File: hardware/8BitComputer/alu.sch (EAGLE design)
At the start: 32 parts, among them IC1 SN74LS245NE4, IC2 SN74LS86AN, IC3 SN74LS283N, IC4 SN74LS86AN, IC8 SN74LS283N

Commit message: alu routed
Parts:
- added LED9: RED, leds:LED-3MM-NO_SILK
- added R9: 100 R, passives:RESISTOR0805-RES
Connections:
- removed net N$6: J5.5
- new net N$10: IC3.C4, R9.1
- new net N$11: LED9.A, R9.2
- net ALUOUT_OE: now also J5.3; no longer J5.2
- net AO_DIR: now also J5.2; no longer J5.3
- net AR2O_2: now also IC8.B3
- net AR2O_3: no longer IC8.B3
- net CARRY_ADD: now also IC3.C0, IC8.C4; no longer IC3.C4, IC8.C0
- net GND: now also J5.5, LED9.C
- net OP_SUBTRACT: now also IC8.C0; no longer IC8.C4
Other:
- note added: "C4 = carry out We subtract by using the 2's compliment, so we need to add one after we create the 1 compliement. X - Y = X + (~Y+1)"
- note removed: "C4 = carry In We subtract by using the 2's compliment, so we need to add one after we create the 1 compliement. X - Y = X + (~Y+1)"
- moved on the sheet: J2

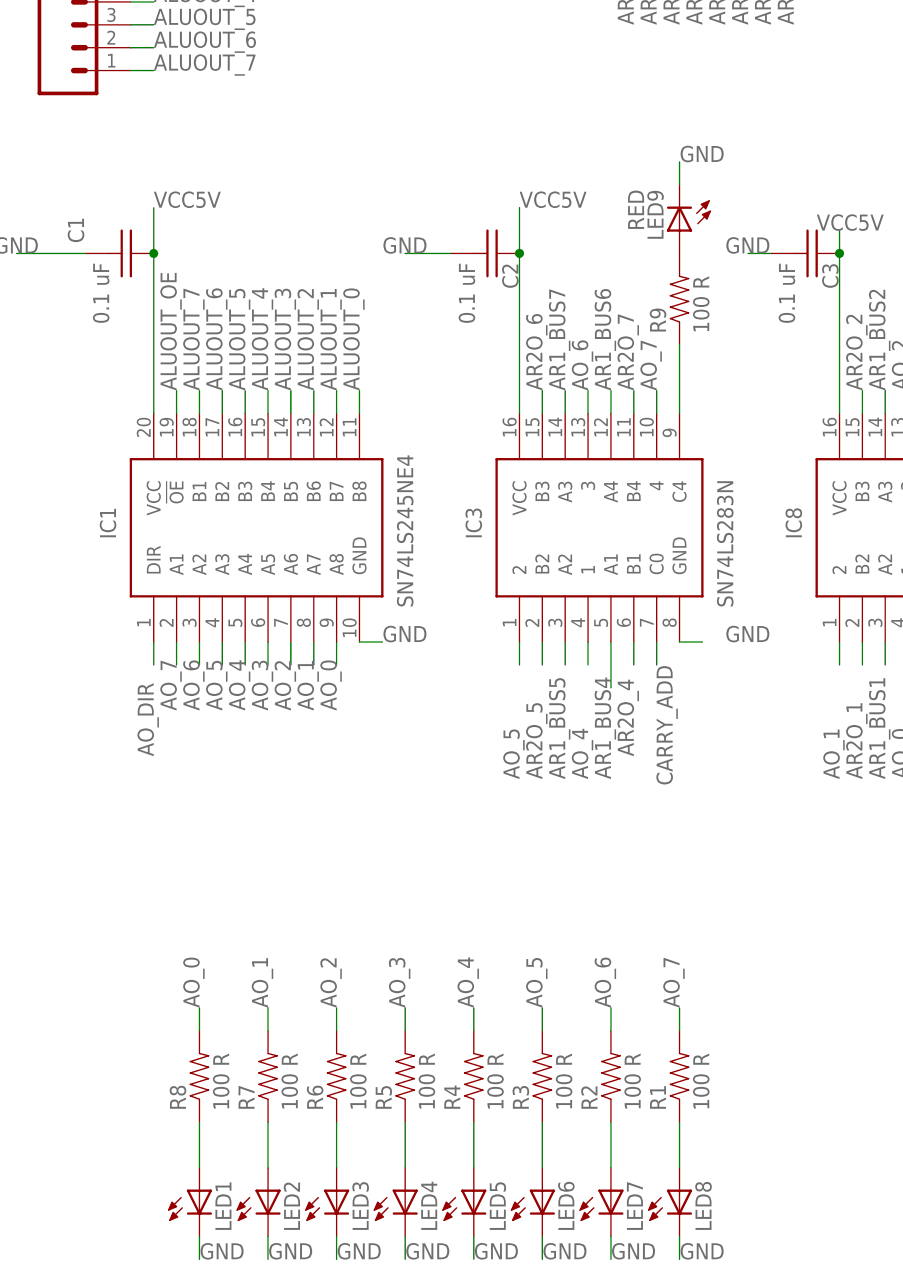
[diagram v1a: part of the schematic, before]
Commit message: adding static ram chip updated all other boards to remove led resistors that aren't needed
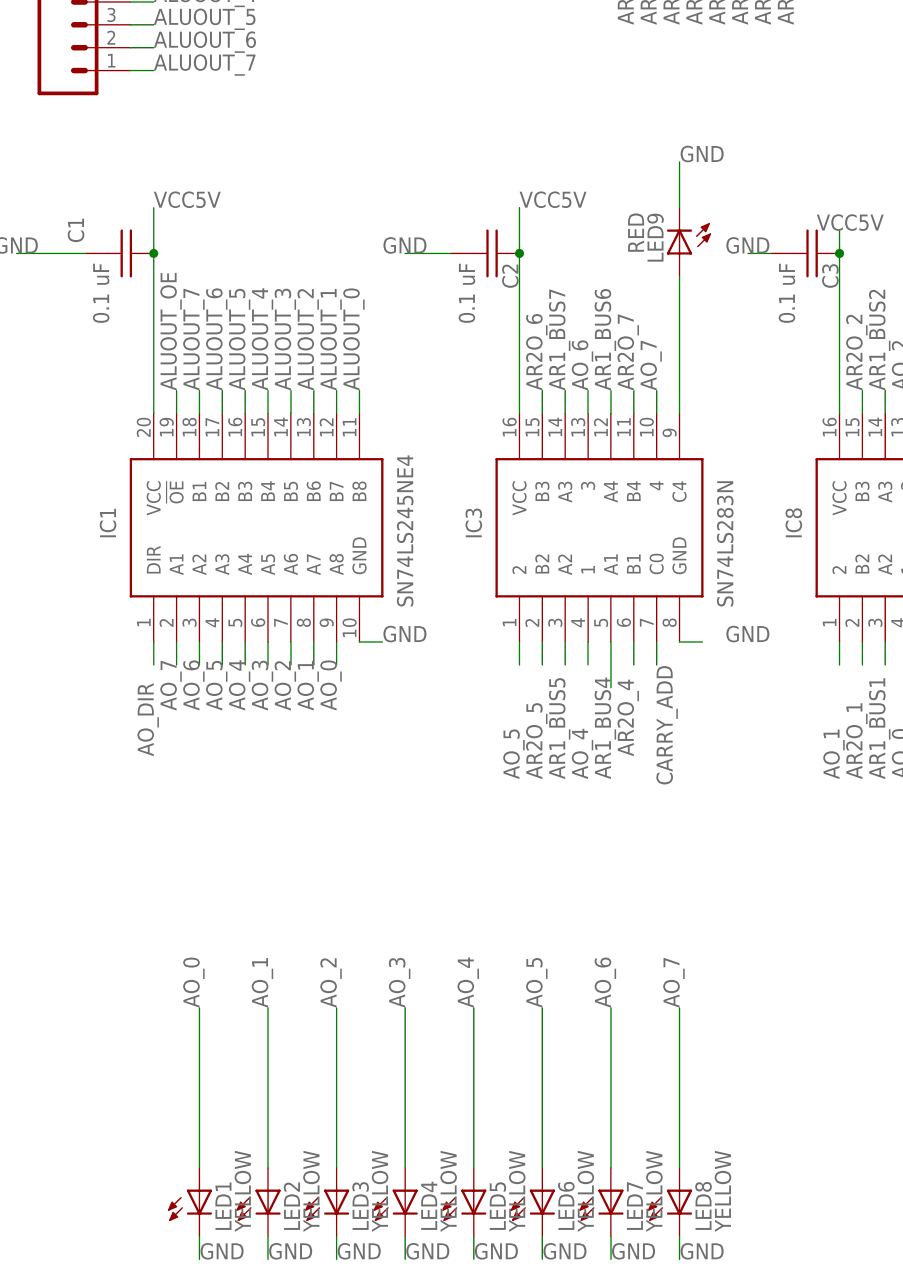
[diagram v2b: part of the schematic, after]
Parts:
- removed R1, R2, R3, R4, R5, R6, R7, R8, R9: 100 R, passives:RESISTOR0805-RES
- LED1, LED2, LED3, LED4, LED5, LED6, LED7, LED8: value (none) -> YELLOW
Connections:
- removed net N$1: LED1.A, R8.1
- removed net N$11: LED9.A, R9.2
- removed net N$2: LED2.A, R7.1
- removed net N$3: LED3.A, R6.1
- removed net N$4: LED4.A, R5.1
- removed net N$5: LED5.A, R4.1
- removed net N$7: LED6.A, R3.1
- removed net N$8: LED7.A, R2.1
- removed net N$9: LED8.A, R1.1
- net AO_0: now also LED1.A; no longer R8.2
- net AO_1: now also LED2.A; no longer R7.2
- net AO_2: now also LED3.A; no longer R6.2
- net AO_3: now also LED4.A; no longer R5.2
- net AO_4: now also LED5.A; no longer R4.2
- net AO_5: now also LED6.A; no longer R3.2
- net AO_6: now also LED7.A; no longer R2.2
- net AO_7: now also LED8.A; no longer R1.2
- net N$10: now also LED9.A; no longer R9.1
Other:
- moved on the sheet: LED9
